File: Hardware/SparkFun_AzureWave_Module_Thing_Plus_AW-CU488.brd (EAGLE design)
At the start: 22.9 x 71.1 mm, 82 parts, among them J3 QWIIC_RA, J5 USB-C, Q1 2.5A/30V, U2 CP210X, U3 AP2112, U4 MCP73831, U5 TC7USB40MU

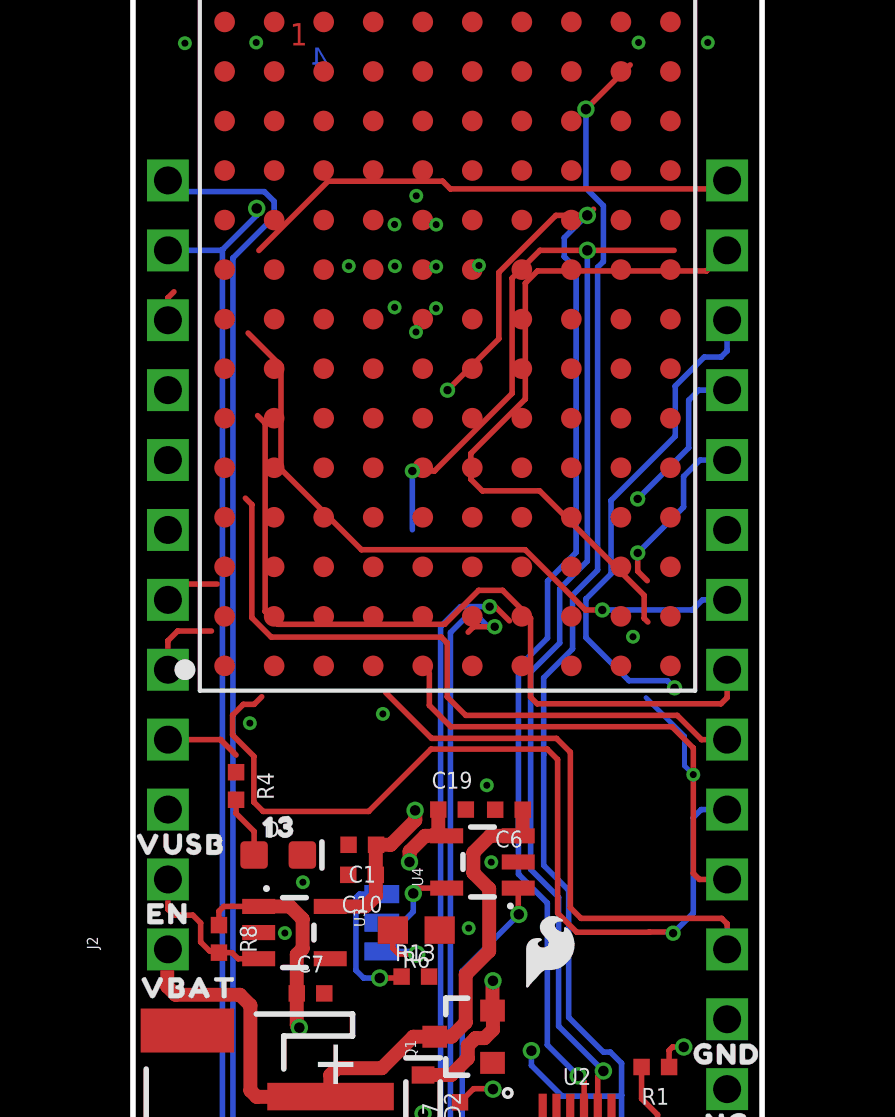
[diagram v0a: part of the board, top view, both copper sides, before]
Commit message: vbat meas connection and some net cleanup
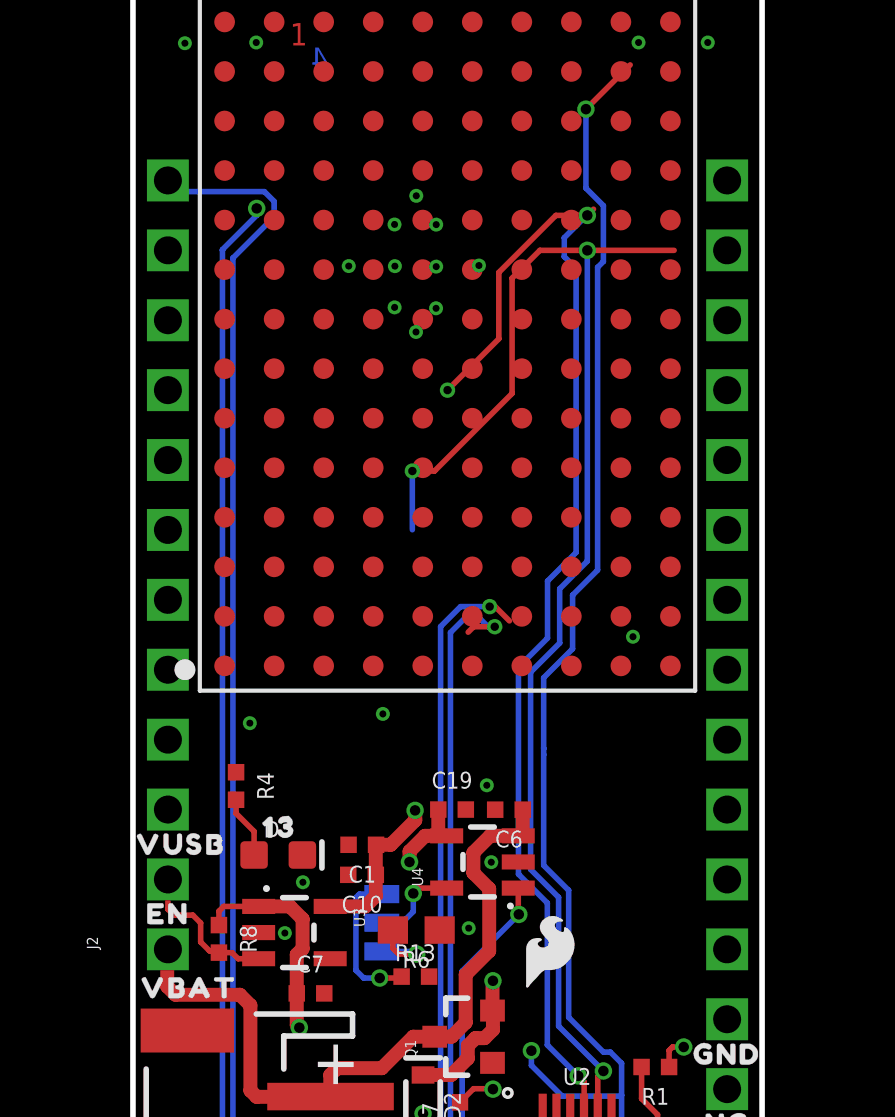
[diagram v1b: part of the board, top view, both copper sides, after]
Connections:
- removed net 10: J2.7
- removed net 11: J2.6
- removed net 12: J2.5
- removed net 13: J2.4
- removed net 3: J4.16
- removed net 33/RX1: J4.14
- removed net 34/TX1: J4.15
- removed net 4: J2.10
- removed net 6: J2.9
- removed net 8: J2.8
- removed net A0: J4.5
- removed net A1: J4.6
- removed net A2: J4.7
- removed net A3: J4.8
- removed net A4: J4.9
- removed net A5: J4.10
- removed net CIPO: J4.13
- removed net COPI: J4.12
- removed net SCK: J4.11
- net SCL: no longer J2.11
- net SDA: no longer J2.12
- net V_BATT: now also U$13.D2
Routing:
- net A2: track 33.0 -> 0.00 mm, vias 1 -> 0
- net A4: track 29.2 -> 0.00 mm
- net 34/TX1: track 24.8 -> 0.00 mm
- net A3: track 24.7 -> 0.00 mm
- net A5: track 23.9 -> 0.00 mm, vias 1 -> 0
- net A1: track 20.8 -> 0.00 mm, vias 1 -> 0
- net A0: track 20.1 -> 0.00 mm
- net 3: track 18.3 -> 0.00 mm
- net 33/RX1: track 18.0 -> 0.00 mm, vias 1 -> 0
- net COPI: track 6.45 -> 0.00 mm, vias 1 -> 0
- net CIPO: track 5.94 -> 0.00 mm, vias 1 -> 0
- net 12: track 2.78 -> 0.00 mm
- net 13: track 2.72 -> 0.00 mm
- net 11: track 2.04 -> 0.00 mm
- net SCL: track 47.6 -> 45.7 mm
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
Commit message: layout almost there
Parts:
- added U$10: (no value), output:THING_PLUS_0
- added U$6, U$8: (no value), output:AZUREWAVE0
- added U$9: (no value), output:AW#CU488_0
- R10, R15: device SparkFun-Resistors:0603 -> SparkFun-Resistors:0402-TIGHT
- moved R16 99.2 mm to (1.27, 55.2), turned to 270 degrees
- moved C4 86.3 mm to (11.4, 31.8), turned to 180 degrees
- moved R10 68.0 mm to (14.5, 20.7), turned to 90 degrees
- moved R14 65.9 mm to (19.4, 7.17)
- moved R15 64.5 mm to (8.51, 14.1), turned to 270 degrees
- moved LOGO3 37.6 mm to (11.6, 63.9)
- moved U$27 19.4 mm to (17.7, 28.4), turned to 90 degrees
- moved U$62 18.6 mm to (19.3, 28.2), turned to 90 degrees
- moved LOGO1 11.1 mm to (6.63, 31.2)
- moved R3 0.49 mm to (19.4, 6.16)
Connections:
- removed net CHIP_PU: J4.1
- removed net PB31: R4.1, U$13.K7
- new net PA0: J4.14, U$13.K8
- new net PA16: J2.10, U$13.A11
- new net PA18: J2.9, U$13.A10
- new net PA2: J4.16, U$13.K10
- new net PA27: J2.8, U$13.A9
- new net PA30: J2.7, U$13.A8
- new net PA4: J4.15, U$13.K9
- new net PB1: J2.5, U$13.A3
- new net PB2: J2.6, U$13.A4
- new net PB22/A4: J4.9, U$13.K1
- new net PB23/A5: J4.10, U$13.K2
- new net PB26/SCK: J4.11, U$13.K5
- new net PB29/PICO: J4.12, U$13.K6
- new net PB3: J2.4, R4.1, U$13.B1
- new net PB31/POCI: J4.13, U$13.K7
- new net PB4/A0: J4.5, U$13.B2
- new net PB5/A1: J4.6, U$13.C1
- new net PB6/A2: J4.7, U$13.C2
- new net PB7/A3: J4.8, U$13.D1
- net CHIP_EN: now also J4.1
- net SCL: now also J2.11, U$13.B12
- net SDA: now also J2.12, U$13.A12
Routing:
- net CHIP_PU: track 60.2 -> 0.00 mm, vias 3 -> 0
- net CHIP_EN: track 0.00 -> 57.2 mm, vias 0 -> 2
- net PB4/A0: track 0.00 -> 24.5 mm, vias 0 -> 2
- net PB5/A1: track 0.00 -> 19.9 mm, vias 0 -> 2
- net PB6/A2: track 0.00 -> 18.7 mm, vias 0 -> 2
- net PB7/A3: track 0.00 -> 15.2 mm, vias 0 -> 2
- net V_BATT: track 27.0 -> 38.4 mm
- net N$12: track 0.00 -> 11.2 mm, vias 0 -> 2
- net PA30: track 0.00 -> 8.80 mm
- net PA25/HSDM: track 31.3 -> 39.7 mm
- net PA27: track 0.00 -> 7.98 mm
- net PA26/HSDP: track 31.5 -> 39.4 mm
- net PB3: track 0.00 -> 7.30 mm
- net PA18: track 0.00 -> 7.22 mm
- net PA7/UART-LOG-TXD: track 50.5 -> 57.6 mm
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
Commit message: Layout done for proto v01
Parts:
- removed J2: (no value), SparkFun-Connectors:1X12_SM_SQ_NOSILK
- removed J4: (no value), SparkFun-Connectors:1X16_SM_SQ_NOSILK
- removed U$75: (no value), output:VUSB0
- removed U$76: (no value), output:EN0
- removed U$77: (no value), output:VBAT0
- removed U$81: (no value), output:3V30
- removed U$82: (no value), output:NC0
- removed U$83: (no value), output:GND0
- added J1: THING_PLUS, SparkFun-Boards:THING_PLUS
- added U$12: (no value), output:#A5#0
- added U$15: (no value), output:#2#0
- added U$16: (no value), output:#3#0
- added U$17: (no value), output:#4#0
- added U$18: (no value), output:#5#0
- added U$19: (no value), output:#A4#0
- added U$20: (no value), output:#6#0
- added U$21: (no value), output:#A2#0
- added U$22: (no value), output:#A3#0
- added U$23: (no value), output:#7#0
- added U$24: (no value), output:#8#0
- added U$25: (no value), output:#9#0
- added U$26: (no value), output:#10#0
- added U$28: (no value), output:#A0#0
- added U$29: (no value), output:#14#SDA#0
- added U$30: (no value), output:#15#SCL#0
- added U$31: (no value), output:#13#SCK#0
- added U$33: (no value), output:#12#PICO#0
- added U$34: (no value), output:#11#POCI#0
- added U$64: (no value), output:#A1#0
- U$7: device output:#RST#0 -> output:#1#0
- moved U$7 39.2 mm to (2.69, 47.0), flipped to the bottom
- moved R7 5.10 mm to (14.8, 22.3), turned to 0 degrees
- moved R10 0.57 mm to (14.8, 21.2), turned to 180 degrees
- moved R12 0.28 mm to (10.3, 14.1)
- moved R15 0.15 mm to (8.36, 14.1)
- moved U$79 0.13 mm to (18.7, 10.4)
- moved U$2 0.13 mm to (9.78, 10.5)
- moved R2 0.13 mm to (9.32, 14.1)
- moved U$78 0.10 mm to (21.8, 9.01)
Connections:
- net 3.3V: now also J1.27; no longer J4.2
- net CHIP_EN: now also J1.28; no longer J4.1
- net EN: now also J1.11; no longer J2.2
- net GND: now also J1.25; no longer J4.4
- net PA0: now also J1.15; no longer J4.14
- net PA16: now also J1.3; no longer J2.10
- net PA18: now also J1.4; no longer J2.9
- net PA2: now also J1.13; no longer J4.16
- net PA27: now also J1.5; no longer J2.8
- net PA30: now also J1.6; no longer J2.7
- net PA4: now also J1.14; no longer J4.15
- net PB1: now also J1.8; no longer J2.5
- net PB2: now also J1.7; no longer J2.6
- net PB22/A4: now also J1.20; no longer J4.9
- net PB23/A5: now also J1.19; no longer J4.10
- net PB26/SCK: now also J1.18; no longer J4.11
- net PB29/PICO: now also J1.17; no longer J4.12
- net PB3: now also J1.9; no longer J2.4
- net PB31/POCI: now also J1.16; no longer J4.13
- net PB4/A0: now also J1.24; no longer J4.5
- net PB5/A1: now also J1.23; no longer J4.6
- net PB6/A2: now also J1.22; no longer J4.7
- net PB7/A3: now also J1.21; no longer J4.8
- net SCL: now also J1.2; no longer J2.11
- net SDA: now also J1.1; no longer J2.12
- net V_BATT: now also J1.12; no longer J2.1
- net V_USB: now also J1.10; no longer J2.3
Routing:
- net PB4/A0: track 24.5 -> 22.8 mm
- net USB_SEL: track 12.9 -> 14.2 mm
- net PB5/A1: track 19.9 -> 18.8 mm
- net V_USB: track 23.1 -> 23.9 mm
- net CHG: track 25.1 -> 24.4 mm
- net PB29/PICO: track 3.30 -> 2.69 mm
- net 3.3V: track 34.8 -> 35.4 mm
- net GND: vias 30 -> 71

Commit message: tweaking for pin functions in progress
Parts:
- removed R2: 10k, SparkFun-Resistors:0402-TIGHT
- removed U5: TC7USB40MU, esp32-s2-wroom:UQFN10
- removed USB: (no value), SparkFun-Jumpers:SMT-JUMPER_3_1-NC_TRACE_SILK
- moved U$13 5.08 mm to (11.4, 54.6)
- moved FD1 3.81 mm to (21.5, 73.5)
- moved FD2 3.81 mm to (21.5, 73.5)
- moved LOGO3 3.81 mm to (11.6, 67.7)
- moved R16 3.81 mm to (1.27, 59.1)
- moved U$10 3.81 mm to (11.4, 60.7)
- moved U$8 3.81 mm to (11.4, 65.0)
- moved U$9 3.81 mm to (11.3, 62.9)
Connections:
- removed net N$3: J5.A6, J5.B6, U5.3
- removed net N$5: J5.A7, J5.B7, U5.5
- removed net N$6: R2.2, USB.1
- removed net PA16: J1.3, U$13.A11
- removed net PA18: J1.4, U$13.A10
- removed net PB1: J1.8, U$13.A3
- removed net PB2: J1.7, U$13.A4
- removed net PB22/A4: J1.20, U$13.K1
- removed net PB23/A5: J1.19, U$13.K2
- removed net PB26/SCK: J1.18, U$13.K5
- removed net PB29/PICO: J1.17, U$13.K6
- removed net PB31/POCI: J1.16, U$13.K7
- removed net PB5/A1: J1.23, U$13.C1
- removed net PB6/A2: J1.22, U$13.C2
- removed net USB_SEL: U5.10, USB.2
- new net PA16/PICO: J1.17, U$13.A11
- new net PA17/POCI: J1.16, U$13.B11
- new net PA18/SCK: J1.18, U$13.A10
- new net PA19/CS: J1.19, U$13.B10
- new net PB1/A4: J1.22, U$13.A3
- new net PB2/A5: J1.21, U$13.A4
- new net PB3/A6: J1.20, U$13.B1
- net 3.3V: no longer R2.1, U5.9
- net CP210X_D+: now also J5.A6, J5.B6; no longer U5.1
- net CP210X_D-: now also J5.A7, J5.B7; no longer U5.7
- net GND: no longer U5.4, U5.8, USB.3
- net PA0: no longer J1.15
- net PA2: no longer J1.13
- net PA25/HSDM: no longer U5.6
- net PA26/HSDP: no longer U5.2
- net PA27: no longer J1.5
- net PA30: no longer J1.6
- net PA4: no longer J1.14
- net PB3: no longer J1.9, U$13.B1
- net PB7/A3: now also J1.23; no longer J1.21
- net SCL: now also U$13.C1; no longer U$13.B12
- net SDA: now also U$13.C2; no longer U$13.A12
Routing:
- net PA25/HSDM: track 39.7 -> 0.00 mm, vias 2 -> 0
- net PA26/HSDP: track 39.4 -> 0.00 mm, vias 2 -> 0
- net PB5/A1: track 18.8 -> 0.00 mm, vias 2 -> 0
- net PB6/A2: track 18.8 -> 0.00 mm, vias 2 -> 0
- net PB7/A3: track 15.2 -> 0.00 mm, vias 2 -> 0
- net USB_SEL: track 14.2 -> 0.00 mm, vias 1 -> 0
- net PA30: track 8.51 -> 0.00 mm
- net PA27: track 7.79 -> 0.00 mm
- net PA18: track 7.26 -> 0.00 mm
- net SCL: track 51.7 -> 44.5 mm
- net PA16: track 6.49 -> 0.00 mm
- net N$5: track 6.03 -> 0.00 mm
- net N$3: track 5.09 -> 0.00 mm, vias 2 -> 0
- net PB4/A0: track 22.8 -> 27.8 mm
- net V_BATT: track 38.4 -> 43.5 mm
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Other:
- board size 22.9 x 71.1 mm -> 22.9 x 74.9 mm

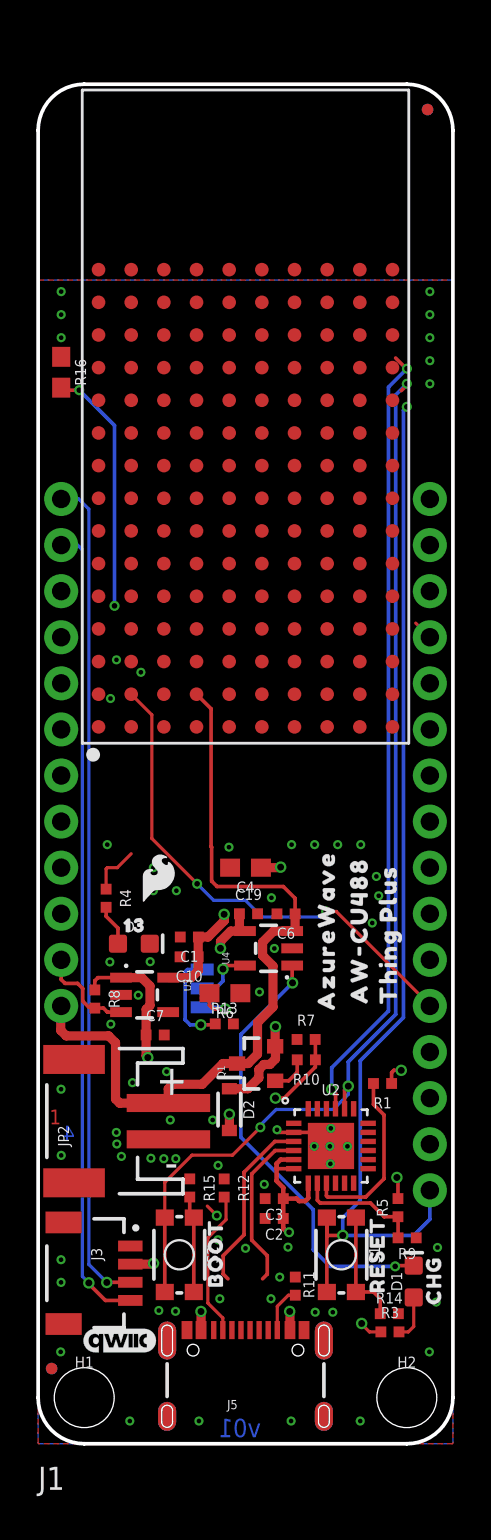
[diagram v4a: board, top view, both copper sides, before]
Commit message: Routed but needs cleanup and silk updates
-added auto-reset back in
-broke out extra GPIO to "bonus" PTH headers on upper sides
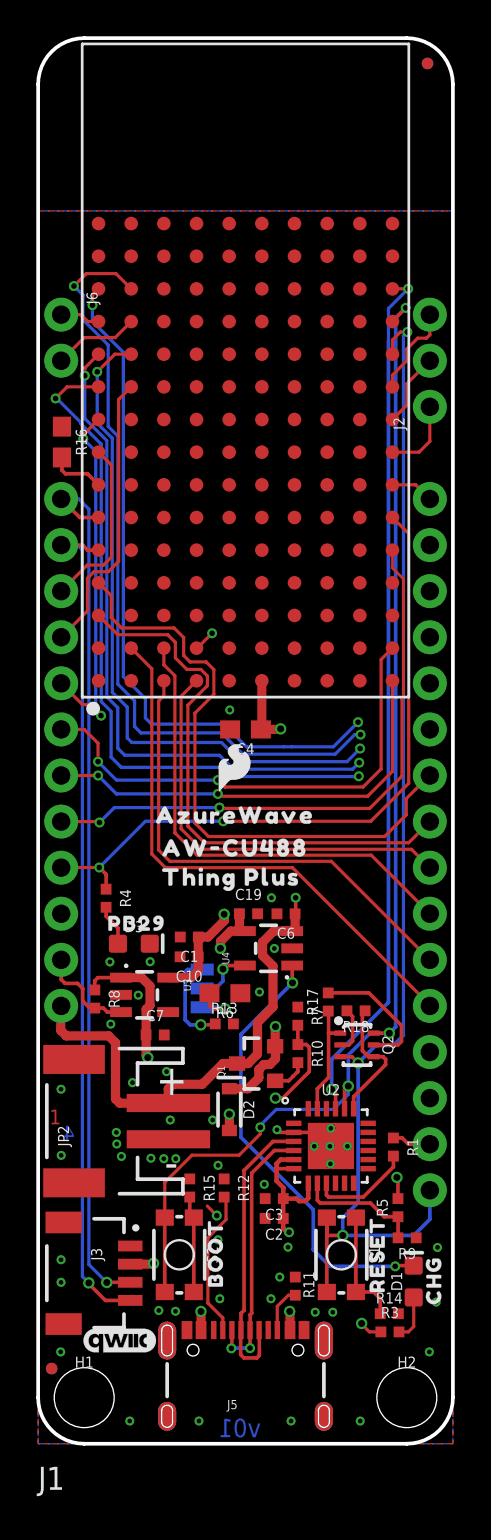
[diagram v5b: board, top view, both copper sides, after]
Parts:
- removed U$74: (no value), output:130
- added J2: (no value), SparkFun-Connectors:1X03_NO_SILK
- added J6: (no value), SparkFun-Connectors:1X02_NO_SILK
- added Q2: MBT3904DW1T1, SparkFun-DiscreteSemi:SC70-6
- added R17, R18: 10k, SparkFun-Resistors:0402-TIGHT
- added U$35: (no value), output:PB290
- moved U$62 9.00 mm to (10.8, 31.2), turned to 0 degrees
- moved U$6 8.11 mm to (10.9, 34.6), turned to 0 degrees
- moved U$27 7.98 mm to (11.0, 32.8), turned to 0 degrees
- moved C4 7.62 mm to (11.4, 39.4)
- moved LOGO1 7.38 mm to (10.8, 37.3)
- moved R16 3.85 mm to (1.31, 55.2)
- moved R1 3.55 mm to (19.6, 16.4), turned to 270 degrees
- moved U$10 2.54 mm to (11.4, 63.2)
- moved U$8 2.54 mm to (11.4, 67.6)
- moved U$9 2.54 mm to (11.3, 65.4)
- moved U$13 2.54 mm to (11.4, 57.1)
- moved FD1 2.54 mm to (21.5, 76.1)
- moved FD2 2.54 mm to (21.5, 76.1)
- moved LOGO3 2.54 mm to (11.6, 70.2)
- moved R7 1.36 mm to (14.3, 23.6), turned to 270 degrees
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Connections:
- removed net PA25/HSDM: U$13.A5
- removed net PA26/HSDP: U$13.A6
- removed net PB3: R4.1
- new net DTR: Q2.1, R17.1, U2.23
- new net LP_UART_RXD: J1.15, U$13.B13
- new net LP_UART_TXD: J1.14, U$13.A13
- new net N$3: Q2.5, R17.2
- new net N$5: Q2.2, R18.2
- new net PA14: J6.1, U$13.A12
- new net PA15: J6.2, U$13.B12
- new net PB22: J1.7, U$13.K1
- new net PB23: J1.6, U$13.K2
- new net PB26: J1.8, U$13.K5
- new net PB29: J1.9, R4.1, U$13.K6
- new net PB31: J1.13, U$13.K7
- new net PB5/A1: J1.23, U$13.C1
- new net PB6/A2: J1.22, U$13.C2
- new net RTS: Q2.4, R18.1, U2.19
- net CHIP_EN: now also Q2.3
- net PA0: now also J2.1
- net PA19/CS: now also J1.4; no longer J1.19
- net PA2: now also J2.3
- net PA27: now also J1.5
- net PA30: now also J1.3
- net PA4: now also J2.2
- net PA7/UART-LOG-TXD: now also Q2.6
- net PB1/A4: now also J1.20; no longer J1.22
- net PB2/A5: now also J1.19; no longer J1.21
- net PB3/A6: no longer J1.20
- net PB7/A3: now also J1.21; no longer J1.23
- net SCL: now also U$13.A5; no longer U$13.C1
- net SDA: now also U$13.A6; no longer U$13.C2
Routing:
- net LP_UART_RXD: track 0.00 -> 52.5 mm, vias 0 -> 2
- net LP_UART_TXD: track 0.00 -> 49.3 mm, vias 0 -> 2
- net PA17/POCI: track 1.10 -> 44.9 mm, vias 0 -> 2
- net PA16/PICO: track 0.00 -> 43.0 mm, vias 0 -> 2
- net PA18/SCK: track 0.20 -> 42.8 mm, vias 0 -> 2
- net PB29: track 0.00 -> 37.5 mm, vias 0 -> 2
- net PB2/A5: track 0.00 -> 33.7 mm
- net PB26: track 0.00 -> 32.6 mm, vias 0 -> 2
- net PB1/A4: track 0.00 -> 30.8 mm
- net PB5/A1: track 0.00 -> 26.9 mm
- net PB23: track 0.00 -> 26.9 mm, vias 0 -> 2
- net PB6/A2: track 0.00 -> 26.3 mm
- net PB22: track 0.00 -> 24.3 mm, vias 0 -> 2
- net PB7/A3: track 0.00 -> 23.1 mm
- net PA27: track 0.00 -> 20.0 mm, vias 0 -> 2
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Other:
- board size 22.9 x 74.9 mm -> 22.9 x 77.5 mm

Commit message: More Layout work - pretty much 99% done
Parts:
- removed LOGO1: SFE_LOGO_FLAME.1_INCH, SparkFun-Aesthetics:SFE_LOGO_FLAME_.1
- removed R16: 12k, SparkFun-Resistors:0603
- removed U$20: (no value), output:#6#0
- removed U$23: (no value), output:#7#0
- removed U$29: (no value), output:#14#SDA#0
- removed U$30: (no value), output:#15#SCL#0
- removed U$64: (no value), output:#A1#0
- added LOGO5: SFE_LOGO_NAME_FLAME.1_INCH, SparkFun-Aesthetics:SFE_LOGO_NAME_FLAME_.1
- added U$36: (no value), output:#PB22#32
- added U$37: (no value), output:#PB26#32
- added U$38: (no value), output:#PB29#32
- added U$39: (no value), output:#PA18#SCK#19
- added U$40: (no value), output:#PA16#PICO#19
- added U$47: (no value), output:#PA17#POCI#19
- added U$51: (no value), output:#PB4#A0#5
- added U$52: (no value), output:#PB5#A1#5
- added U$53: (no value), output:#A1#6
- added U$54: (no value), output:#A2#6
- added U$55: (no value), output:#A3#6
- added U$56: (no value), output:#A4#6
- added U$57: (no value), output:#A5#6
- added U$58: (no value), output:#PA18#6
- added U$61: (no value), output:#PB6#A2#19
- added U$63: (no value), output:#PB7#A3#19
- added U$65: (no value), output:#PB1#A4#19
- added U$66: (no value), output:#PB2#A5#19
- U$1: device output:#CP210X#0 -> output:#PA13#RXD#19
- U$12: device output:#A5#0 -> output:#PA0#32
- U$14: device output:USB0 -> output:#PB31#19
- U$15: device output:#2#0 -> output:#PB26#30
- U$16: device output:#3#0 -> output:#PB22#30
- U$17: device output:#4#0 -> output:#PB23#30
- U$18: device output:#5#0 -> output:#A0#30
- U$19: device output:#A4#0 -> output:#PA4#32
- U$21: device output:#A2#0 -> output:#PA2#32
- U$22: device output:#A3#0 -> output:#PA14#32
- U$24: device output:#8#0 -> output:#PA15#32
- U$25: device output:#9#0 -> output:#PA26#SDA#32
- U$26: device output:#10#0 -> output:#PA25#SCL#32
- U$28: device output:#A0#0 -> output:#PA30#32
- U$31: device output:#13#SCK#0 -> output:#PA19#CS#32
- U$33: device output:#12#PICO#0 -> output:#PA27#32
- U$34: device output:#11#POCI#0 -> output:#PB23#32
- U$5: device output:#CU488#0 -> output:#PA12#TXD#19
- U$7: device output:#1#0 -> output:#PB29#0
- moved U$14 39.9 mm to (18.7, 52.0), turned to 0 degrees
- moved U$1 36.4 mm to (16.6, 46.9), turned to 0 degrees
- moved U$22 35.0 mm to (4.27, 62.3)
- moved U$5 33.3 mm to (16.6, 49.5), turned to 0 degrees
- moved U$21 33.2 mm to (18.9, 62.2)
- moved U$28 28.4 mm to (4.32, 47.0)
- moved U$19 25.5 mm to (18.9, 59.7)
- moved U$18 21.0 mm to (19.5, 24.1), flipped to the top
- moved U$12 20.5 mm to (18.9, 57.1)
- moved U$24 17.5 mm to (4.21, 59.7)
- moved U$7 15.3 mm to (4.21, 31.7), flipped to the top
- moved U$34 14.6 mm to (4.22, 39.4)
- moved U$25 14.0 mm to (6.21, 52.1)
- moved U$26 13.8 mm to (6.14, 49.5)
- moved U$31 13.6 mm to (5.54, 44.4)
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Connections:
- net SCL renamed PA25/SCL
- net SDA renamed PA26/SDA
- removed net N$12: R16.2, U$13.A7
- removed net PB3/A6: U$13.B1
- net GND: no longer R16.1
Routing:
- net 3.3V: track 34.7 -> 31.3 mm, vias 5 -> 4
- net N$12: track 3.25 -> 0.00 mm
- net PB1/A4: track 30.8 -> 32.9 mm
- net PB2/A5: track 33.7 -> 35.7 mm
- net DTR: track 6.30 -> 8.28 mm
- net PB7/A3: track 23.1 -> 24.8 mm
- net PB6/A2: track 26.3 -> 28.0 mm
- net PA16/PICO: track 43.0 -> 41.4 mm
- net PA18/SCK: track 42.8 -> 41.2 mm
- net PA17/POCI: track 44.9 -> 43.6 mm
- net PA7/UART-LOG-TXD: track 67.0 -> 68.2 mm
- net PA8/UART-LOG-RXD: track 47.9 -> 49.1 mm
- net PB22: track 24.3 -> 25.4 mm
- net PB29: track 37.5 -> 38.5 mm
- net PB23: track 26.9 -> 27.9 mm
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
